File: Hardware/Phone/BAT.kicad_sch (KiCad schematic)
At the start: 13 parts, among them Q2 AO3400A, Q3 AO3400A

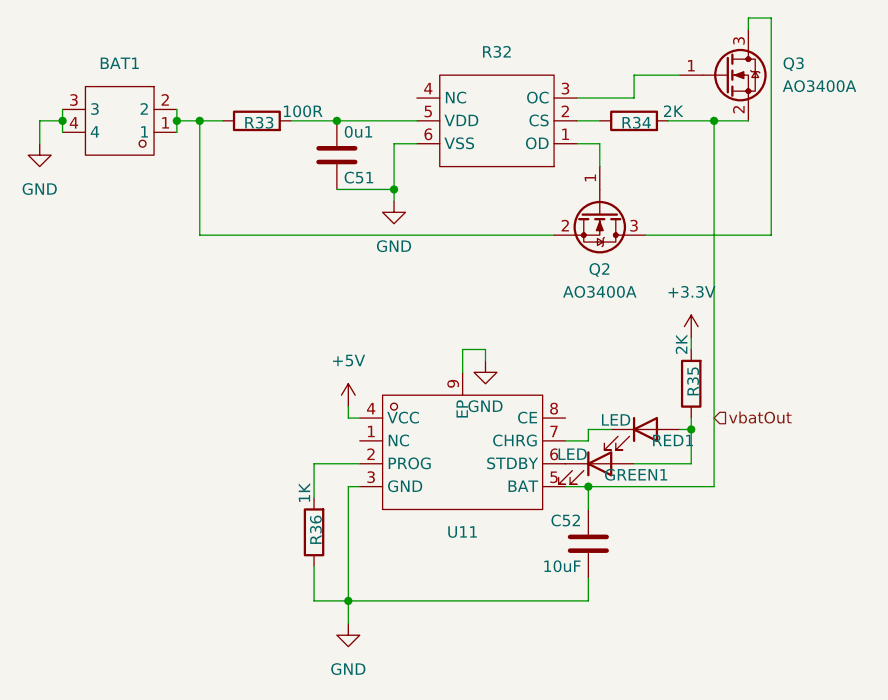
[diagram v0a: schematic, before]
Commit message: added doku. Abendoning Projekt
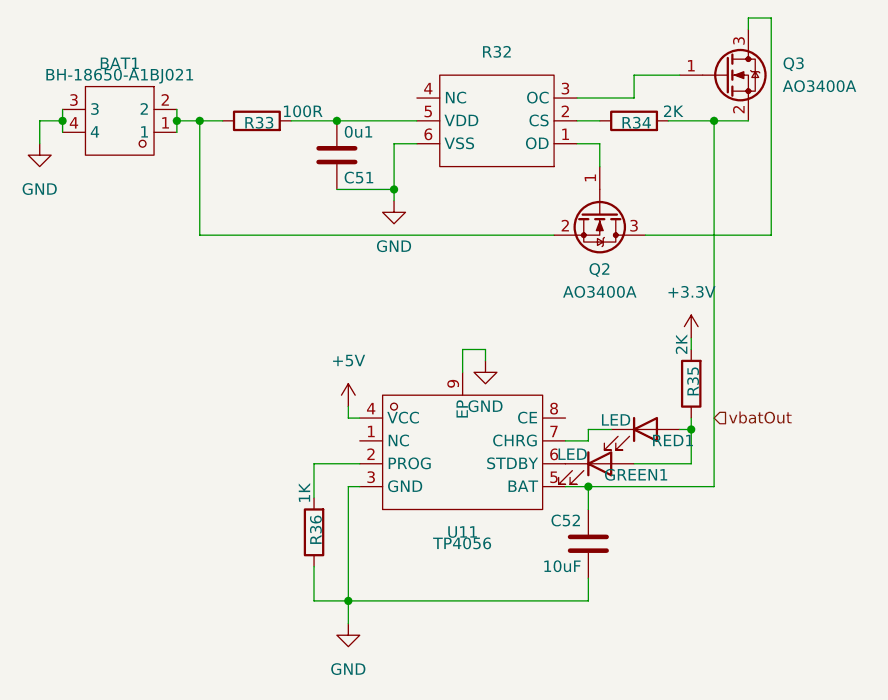
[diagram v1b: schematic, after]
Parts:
- BAT1: value ~ -> BH-18650-A1BJ021
- U11: value ~ -> TP4056
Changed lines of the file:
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@@
 			)
 		)
-		(property "Value" "~"
+		(property "Value" "BH-18650-A1BJ021 "
 			(at 104.14 66.04 0)
 			(effects
@@
 			)
 		)
-		(property "Value" "~"
+		(property "Value" "TP4056 "
 			(at 142.24 118.11 0)
 			(effects
